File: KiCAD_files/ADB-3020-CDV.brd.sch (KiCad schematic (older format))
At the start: 115 parts, among them IC1 7812T, IC2 NE5532N, IC3 LM2576, IC4 NE555, IC5 IR2184D, J1 + IN, J2 - IN, J3 + OUT, J4 PIN2F061.040, J5 + IN, J6 - IN, J7 PIN2F061.040, J8 - OUT, Q1 IRFP4310ZPBF, Q2 IRFP4310ZPBF, Q4 BDX53, T1 BC337, T2 BC337

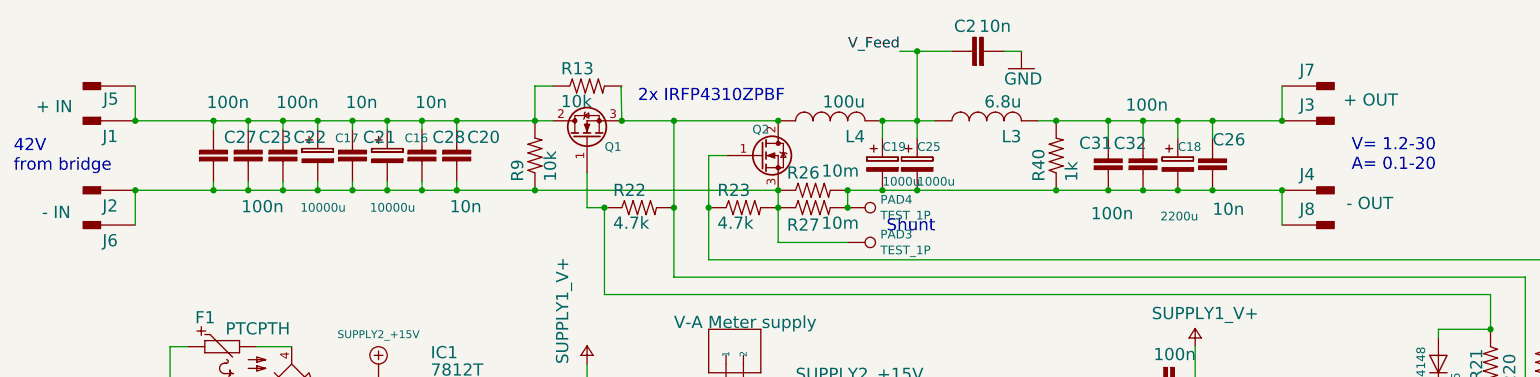
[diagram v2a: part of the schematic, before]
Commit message: Completed layout
* added last footprints
* added silkscreen wordings
* adedd logos
* added soldermask zones
* fixed component identifier positions 


Missing:
* Schematic description in sch file
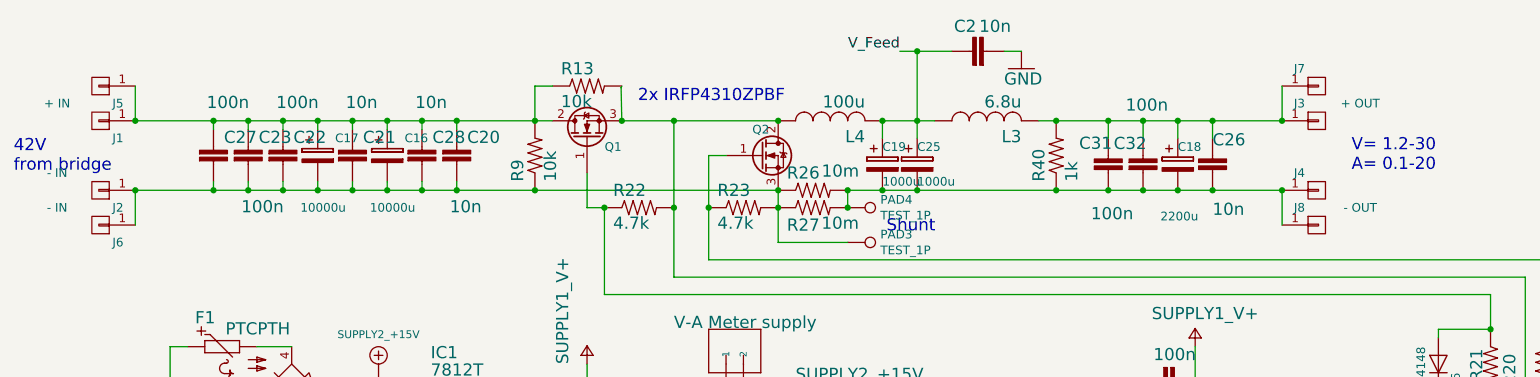
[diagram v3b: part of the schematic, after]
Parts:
- removed J1, J5: + IN, symbol CON-FASTON_PIN2F061.040
- removed J2, J6: - IN, symbol CON-FASTON_PIN2F061.040
- removed J3: + OUT, symbol CON-FASTON_PIN2F061.040
- removed J4, J7: PIN2F061.040, symbol CON-FASTON_PIN2F061.040
- removed J8: - OUT, symbol CON-FASTON_PIN2F061.040
- added J1, J5: + IN, customparts:faston_6.3mm, symbol CONN_01X01
- added J2, J6: - IN, customparts:faston_6.3mm, symbol CONN_01X01
- added J3, J7: + OUT, customparts:faston_6.3mm, symbol CONN_01X01
- added J4, J8: - OUT, customparts:faston_6.3mm, symbol CONN_01X01
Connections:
- net at C16.1, C17.1, C20.1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: now also J1.1 (P1), J5.1 (P1)
- net at C16.2, C17.2, C20.2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: now also J2.1 (P1), J6.1 (P1)
- net at C18.1, C26.1, C31.1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: now also J3.1 (P1), J7.1 (P1)
- net at C18.2, C19.2, C25.2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: now also J4.1 (P1), J8.1 (P1)
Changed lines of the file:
@@
-$EndComp
-$Comp
-L CON-FASTON_PIN2F061.040 J1
-U 1 1 59A095ED
-P 1400 1100
-F 0 "J1" H 1300 1149 70  0000 L BNN
-F 1 "+ IN" H 1390 990 65  0001 L TNN
-F 2 "" H 1390 890 65  0001 L TNN
-F 3 "" H 1400 1100 60  0001 C CNN
-	1    1400 1100
-	-1   0    0    1
-$EndComp
-$Comp
-L CON-FASTON_PIN2F061.040 J2
-U 1 1 59A096B5
-P 1400 1500
-F 0 "J2" H 1300 1549 70  0000 L BNN
-F 1 "- IN" H 1572 1586 70  0000 L BNN
-F 2 "" H 1390 1290 65  0001 L TNN
-F 3 "" H 1400 1500 60  0001 C CNN
-	1    1400 1500
-	-1   0    0    1
-$EndComp
-$Comp
-L CON-FASTON_PIN2F061.040 J3
-U 1 1 59A0977D
-P 8400 1100
-F 0 "J3" H 8300 1150 70  0000 L BNN
-F 1 "+ OUT" H 8552 1179 70  0000 L BNN
-F 2 "" H 8390 890 65  0001 L TNN
-F 3 "" H 8400 1100 60  0001 C CNN
-	1    8400 1100
-	1    0    0    -1
-$EndComp
-$Comp
-L CON-FASTON_PIN2F061.040 J4
-U 1 1 59A09845
-P 8400 1500
-F 0 "J4" H 8300 1550 70  0000 L BNN
-F 1 "PIN2F061.040" H 8390 1390 65  0001 L TNN
-F 2 "" H 8390 1290 65  0001 L TNN
-F 3 "" H 8400 1500 60  0001 C CNN
-	1    8400 1500
-	1    0    0    -1
-$EndComp
-$Comp
-L CON-FASTON_PIN2F061.040 J5
-U 1 1 59A0990D
-P 1400 900
-F 0 "J5" H 1296 934 70  0000 L BNN
-F 1 "+ IN" H 1561 977 70  0000 L BNN
-F 2 "" H 1390 690 65  0001 L TNN
-F 3 "" H 1400 900 60  0001 C CNN
-	1    1400 900
-	-1   0    0    1
-$EndComp
-$Comp
-L CON-FASTON_PIN2F061.040 J6
-U 1 1 59A099D5
-P 1400 1700
-F 0 "J6" H 1300 1749 70  0000 L BNN
-F 1 "- IN" H 1390 1590 65  0001 L TNN
-F 2 "" H 1390 1490 65  0001 L TNN
-F 3 "" H 1400 1700 60  0001 C CNN
-	1    1400 1700
-	-1   0    0    1
-$EndComp
-$Comp
-L CON-FASTON_PIN2F061.040 J7
-U 1 1 59A09A9D
-P 8400 900
-F 0 "J7" H 8300 950 70  0000 L BNN
-F 1 "PIN2F061.040" H 8390 790 65  0001 L TNN
-F 2 "" H 8390 690 65  0001 L TNN
-F 3 "" H 8400 900 60  0001 C CNN
-	1    8400 900
-	1    0    0    -1
-$EndComp
-$Comp
-L CON-FASTON_PIN2F061.040 J8
-U 1 1 59A09B65
-P 8400 1700
-F 0 "J8" H 8300 1750 70  0000 L BNN
-F 1 "- OUT" H 8570 1784 70  0000 L BNN
-F 2 "" H 8390 1490 65  0001 L TNN
-F 3 "" H 8400 1700 60  0001 C CNN
-	1    8400 1700
-	1    0    0    -1
 $EndComp
 $Comp
@@
 	0    -1   -1   0
 $EndComp
+$Comp
+L CONN_01X01 J5
+U 1 1 59A44FB7
+P 1400 900
+F 0 "J5" H 1300 1000 50  0000 C CNN
+F 1 "+ IN" H 1319 766 50  0001 C CNN
+F 2 "customparts:faston_6.3mm" H 1400 900 50  0001 C CNN
+F 3 "" H 1400 900 50  0001 C CNN
+	1    1400 900
+	-1   0    0    1
+$EndComp
+$Comp
+L CONN_01X01 J1
+U 1 1 59A45321
+P 1400 1100
+F 0 "J1" H 1300 1200 50  0000 C CNN
+F 1 "+ IN" H 1650 1000 50  0000 C CNN
+F 2 "customparts:faston_6.3mm" H 1400 1100 50  0001 C CNN
+F 3 "" H 1400 1100 50  0001 C CNN
+	1    1400 1100
+	-1   0    0    1
+$EndComp
+$Comp
+L CONN_01X01 J2
+U 1 1 59A47DBE
+P 1400 1500
+F 0 "J2" H 1300 1600 50  0000 C CNN
+F 1 "- IN" H 1650 1400 50  0000 C CNN
+F 2 "customparts:faston_6.3mm" H 1400 1500 50  0001 C CNN
+F 3 "" H 1400 1500 50  0001 C CNN
+	1    1400 1500
+	-1   0    0    1
+$EndComp
+$Comp
+L CONN_01X01 J6
+U 1 1 59A47ECE
+P 1400 1700
+F 0 "J6" H 1300 1800 50  0000 C CNN
+F 1 "- IN" H 1650 1600 50  0000 C CNN
+F 2 "customparts:faston_6.3mm" H 1400 1700 50  0001 C CNN
+F 3 "" H 1400 1700 50  0001 C CNN
+	1    1400 1700
+	-1   0    0    1
+$EndComp
+$Comp
+L CONN_01X01 J8
+U 1 1 59A4BF1C
+P 8400 1700
+F 0 "J8" H 8300 1800 50  0000 C CNN
+F 1 "- OUT" H 8319 1566 50  0001 C CNN
+F 2 "customparts:faston_6.3mm" H 8400 1700 50  0001 C CNN
+F 3 "" H 8400 1700 50  0001 C CNN
+	1    8400 1700
+	1    0    0    -1
+$EndComp
+$Comp
+L CONN_01X01 J4
+U 1 1 59A4BF23
+P 8400 1500
+F 0 "J4" H 8300 1600 50  0000 C CNN
+F 1 "- OUT" H 8650 1400 50  0000 C CNN
+F 2 "customparts:faston_6.3mm" H 8400 1500 50  0001 C CNN
+F 3 "" H 8400 1500 50  0001 C CNN
+	1    8400 1500
+	1    0    0    -1
+$EndComp
+$Comp
+L CONN_01X01 J3
+U 1 1 59A4BF2A
+P 8400 1100
+F 0 "J3" H 8300 1200 50  0000 C CNN
+F 1 "+ OUT" H 8650 1000 50  0001 C CNN
+F 2 "customparts:faston_6.3mm" H 8400 1100 50  0001 C CNN
+F 3 "" H 8400 1100 50  0001 C CNN
+	1    8400 1100
+	1    0    0    -1
+$EndComp
+$Comp
+L CONN_01X01 J7
+U 1 1 59A4BF31
+P 8400 900
+F 0 "J7" H 8300 1000 50  0000 C CNN
+F 1 "+ OUT" H 8650 800 50  0000 C CNN
+F 2 "customparts:faston_6.3mm" H 8400 900 50  0001 C CNN
+F 3 "" H 8400 900 50  0001 C CNN
+	1    8400 900
+	1    0    0    -1
+$EndComp
 $EndSCHEMATC
